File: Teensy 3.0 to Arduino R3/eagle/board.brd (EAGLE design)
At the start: 100 x 55.9 mm, 28 parts, among them IC1 7805TV

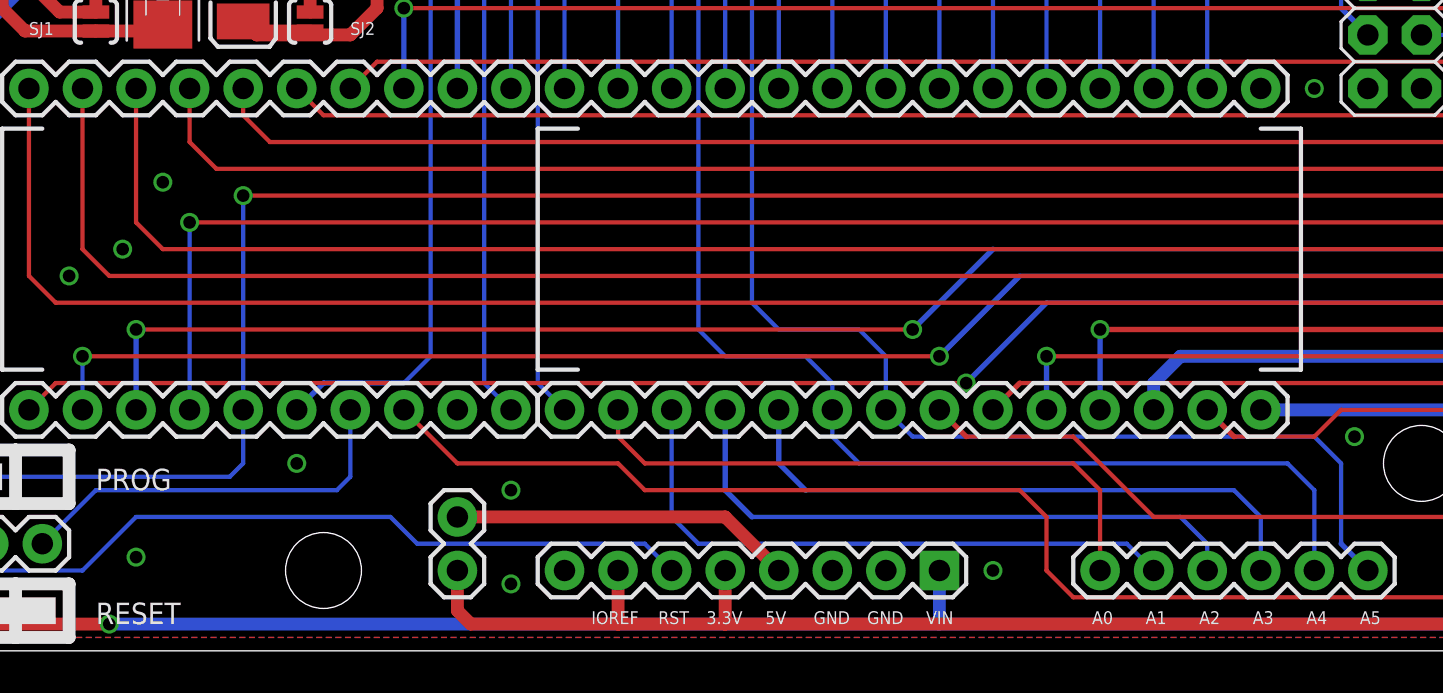
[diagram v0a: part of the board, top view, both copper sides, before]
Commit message: update Arduino R3 board
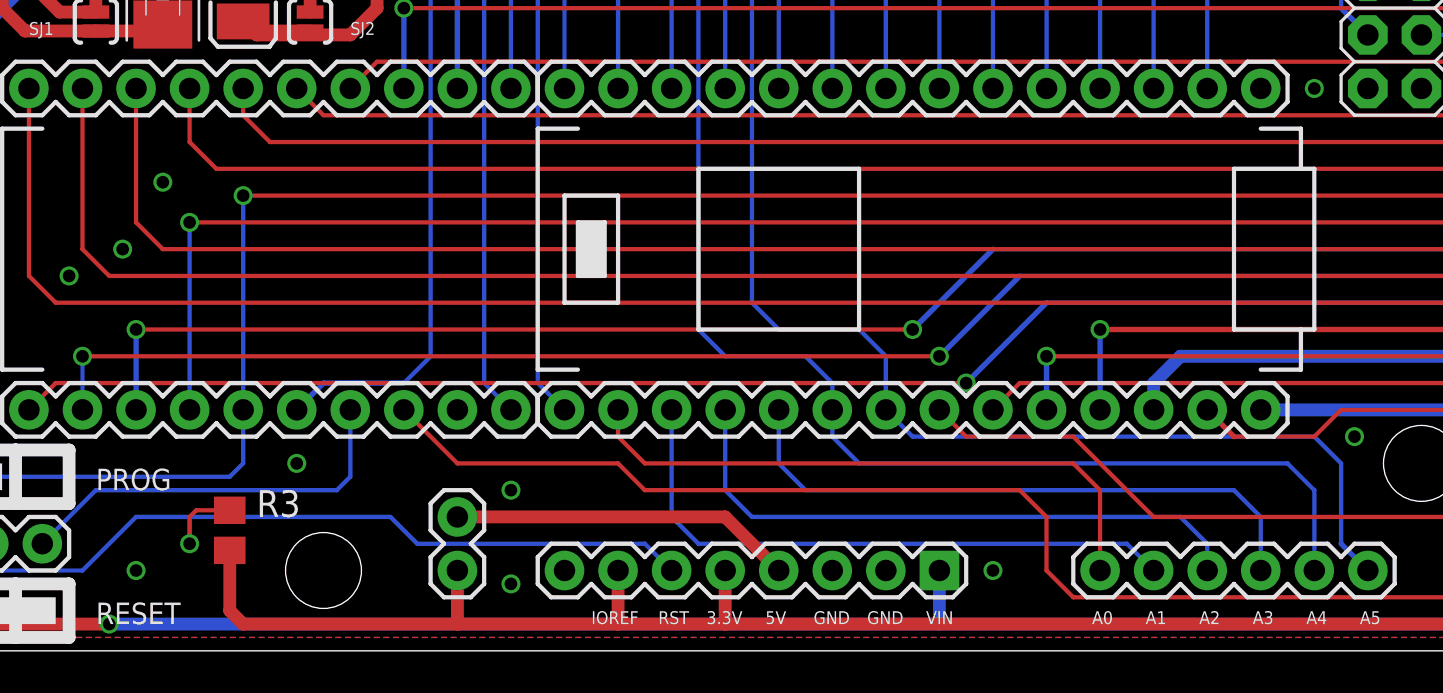
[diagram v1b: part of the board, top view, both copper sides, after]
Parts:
- added R3: (no value), rcl:R0805
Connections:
- net 3V3: now also R3.2
- net EXT_RESET: now also R3.1
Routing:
- net 3V3: track 275.3 -> 289.5 mm
- net EXT_RESET: track 49.5 -> 54.1 mm, vias 0 -> 1
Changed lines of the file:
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@@
 <wire x1="29.21" y1="50.165" x2="35.56" y2="50.165" width="0.2032" layer="21"/>
 <wire x1="35.56" y1="50.165" x2="35.56" y2="43.815" width="0.2032" layer="21"/>
-<wire x1="75.565" y1="24.765" x2="75.565" y2="13.335" width="0.2032" layer="21"/>
 <wire x1="75.565" y1="13.335" x2="73.66" y2="13.335" width="0.2032" layer="21"/>
 <wire x1="75.565" y1="24.765" x2="73.66" y2="24.765" width="0.2032" layer="21"/>
@@
 <text x="34.925" y="36.195" size="0.6096" layer="21">GND</text>
 <text x="34.925" y="33.655" size="0.6096" layer="21">VOUT</text>
+<wire x1="76.2" y1="22.86" x2="75.565" y2="22.86" width="0.2032" layer="21"/>
+<wire x1="75.565" y1="22.86" x2="72.39" y2="22.86" width="0.2032" layer="21"/>
+<wire x1="72.39" y1="22.86" x2="72.39" y2="15.24" width="0.2032" layer="21"/>
+<wire x1="76.2" y1="22.86" x2="76.2" y2="15.24" width="0.2032" layer="21"/>
+<wire x1="75.565" y1="24.765" x2="75.565" y2="22.86" width="0.2032" layer="21"/>
+<wire x1="40.64" y1="21.59" x2="40.64" y2="16.51" width="0.2032" layer="21"/>
+<wire x1="40.64" y1="16.51" x2="43.18" y2="16.51" width="0.2032" layer="21"/>
+<wire x1="43.18" y1="16.51" x2="43.18" y2="21.59" width="0.2032" layer="21"/>
+<wire x1="43.18" y1="21.59" x2="40.64" y2="21.59" width="0.2032" layer="21"/>
+<wire x1="41.275" y1="17.78" x2="42.545" y2="17.78" width="0.2032" layer="21"/>
+<wire x1="42.545" y1="17.78" x2="42.545" y2="20.32" width="0.2032" layer="21"/>
+<wire x1="42.545" y1="20.32" x2="41.275" y2="20.32" width="0.2032" layer="21"/>
+<wire x1="41.275" y1="20.32" x2="41.275" y2="17.78" width="0.2032" layer="21"/>
+<rectangle x1="41.275" y1="17.78" x2="42.545" y2="20.32" layer="21"/>
+<wire x1="46.99" y1="15.24" x2="54.61" y2="15.24" width="0.2032" layer="21"/>
+<wire x1="54.61" y1="15.24" x2="54.61" y2="22.86" width="0.2032" layer="21"/>
+<wire x1="54.61" y1="22.86" x2="46.99" y2="22.86" width="0.2032" layer="21"/>
+<wire x1="46.99" y1="22.86" x2="46.99" y2="15.24" width="0.2032" layer="21"/>
+<wire x1="72.39" y1="15.24" x2="75.565" y2="15.24" width="0.2032" layer="21"/>
+<wire x1="75.565" y1="15.24" x2="76.2" y2="15.24" width="0.2032" layer="21"/>
+<wire x1="75.565" y1="15.24" x2="75.565" y2="13.335" width="0.2032" layer="21"/>
 </plain>
 <attributes>
@@
 <attribute name="VALUE" x="38.735" y="2.54" size="1.27" layer="27" rot="R90"/>
 </element>
+<element name="R3" library="rcl" package="R0805" value="" x="24.765" y="5.715" smashed="yes" rot="R270">
+<attribute name="NAME" x="26.035" y="6.35" size="1.27" layer="25"/>
+<attribute name="VALUE" x="22.225" y="6.35" size="1.27" layer="27" rot="R270"/>
+</element>
 </elements>
 <signals>
@@
 <via x="60.96" y="3.81" extent="1-16" drill="0.6" shape="octagon"/>
 <via x="38.1" y="7.62" extent="1-16" drill="0.6" shape="octagon"/>
-<via x="20.32" y="4.445" extent="1-16" drill="0.6" shape="octagon"/>
 <via x="27.94" y="8.89" extent="1-16" drill="0.6" shape="octagon"/>
 <via x="17.145" y="17.78" extent="1-16" drill="0.6" shape="octagon"/>
@@
 <via x="75.565" y="35.56" extent="1-16" drill="0.6" shape="octagon"/>
 <via x="21.59" y="22.225" extent="1-16" drill="0.6" shape="octagon"/>
+<via x="20.32" y="3.81" extent="1-16" drill="0.6" shape="octagon"/>
 </signal>
 <signal name="D0">
@@
 <wire x1="43.18" y1="1.27" x2="43.18" y2="3.81" width="0.6096" layer="1"/>
 <wire x1="48.26" y1="3.81" x2="48.26" y2="1.27" width="0.6096" layer="1"/>
-<wire x1="35.56" y1="3.81" x2="35.56" y2="1.905" width="0.6096" layer="1"/>
-<wire x1="35.56" y1="1.905" x2="36.195" y2="1.27" width="0.6096" layer="1"/>
-<wire x1="36.195" y1="1.27" x2="43.18" y2="1.27" width="0.6096" layer="1"/>
+<contactref element="R3" pad="2"/>
+<wire x1="43.18" y1="1.27" x2="35.56" y2="1.27" width="0.6096" layer="1"/>
+<wire x1="35.56" y1="1.27" x2="25.4" y2="1.27" width="0.6096" layer="1"/>
+<wire x1="25.4" y1="1.27" x2="24.765" y2="1.905" width="0.6096" layer="1"/>
+<wire x1="24.765" y1="1.905" x2="24.765" y2="4.765" width="0.6096" layer="1"/>
+<wire x1="35.56" y1="3.81" x2="35.56" y2="1.27" width="0.6096" layer="1"/>
 </signal>
 <signal name="A9">
@@
 <wire x1="92.71" y1="10.16" x2="90.17" y2="12.7" width="0.2032" layer="1"/>
 <wire x1="90.17" y1="12.7" x2="62.23" y2="12.7" width="0.2032" layer="1"/>
-<wire x1="62.23" y1="12.7" x2="60.96" y2="11.43" width="0.254" layer="1"/>
+<wire x1="62.23" y1="12.7" x2="60.96" y2="11.43" width="0.2032" layer="1"/>
 <contactref element="JP13" pad="3"/>
 <wire x1="96.52" y1="11.43" x2="95.25" y2="10.16" width="0.2032" layer="1"/>
@@
 <wire x1="68.58" y1="6.35" x2="64.77" y2="10.16" width="0.2032" layer="1"/>
 <wire x1="64.77" y1="10.16" x2="59.69" y2="10.16" width="0.2032" layer="1"/>
-<wire x1="59.69" y1="10.16" x2="58.42" y2="11.43" width="0.254" layer="1"/>
+<wire x1="59.69" y1="10.16" x2="58.42" y2="11.43" width="0.2032" layer="1"/>
 <wire x1="68.58" y1="6.35" x2="88.9" y2="6.35" width="0.2032" layer="1"/>
 <wire x1="88.9" y1="6.35" x2="90.17" y2="7.62" width="0.2032" layer="1"/>
@@
 <wire x1="73.66" y1="6.35" x2="72.39" y2="7.62" width="0.2032" layer="16"/>
 <wire x1="72.39" y1="7.62" x2="52.07" y2="7.62" width="0.2032" layer="16"/>
-<wire x1="52.07" y1="7.62" x2="50.8" y2="8.89" width="0.254" layer="16"/>
-<wire x1="50.8" y1="8.89" x2="50.8" y2="11.43" width="0.254" layer="16"/>
+<wire x1="52.07" y1="7.62" x2="50.8" y2="8.89" width="0.2032" layer="16"/>
+<wire x1="50.8" y1="8.89" x2="50.8" y2="11.43" width="0.2032" layer="16"/>
 </signal>
 <signal name="A2">
@@
 <wire x1="71.12" y1="5.08" x2="69.85" y2="6.35" width="0.2032" layer="16"/>
 <wire x1="69.85" y1="6.35" x2="49.53" y2="6.35" width="0.2032" layer="16"/>
-<wire x1="49.53" y1="6.35" x2="48.26" y2="7.62" width="0.254" layer="16"/>
-<wire x1="48.26" y1="7.62" x2="48.26" y2="11.43" width="0.254" layer="16"/>
+<wire x1="49.53" y1="6.35" x2="48.26" y2="7.62" width="0.2032" layer="16"/>
+<wire x1="48.26" y1="7.62" x2="48.26" y2="11.43" width="0.2032" layer="16"/>
 </signal>
 <signal name="A1">
@@
 <wire x1="44.45" y1="5.08" x2="33.655" y2="5.08" width="0.2032" layer="16"/>
 <wire x1="33.655" y1="5.08" x2="32.385" y2="6.35" width="0.2032" layer="16"/>
-<wire x1="32.385" y1="6.35" x2="20.32" y2="6.35" width="0.2032" layer="16"/>
+<wire x1="32.385" y1="6.35" x2="22.86" y2="6.35" width="0.2032" layer="16"/>
+<contactref element="R3" pad="1"/>
+<wire x1="22.86" y1="6.35" x2="20.32" y2="6.35" width="0.2032" layer="16"/>
+<wire x1="24.765" y1="6.665" x2="23.175" y2="6.665" width="0.2032" layer="1"/>
+<wire x1="23.175" y1="6.665" x2="22.86" y2="6.35" width="0.2032" layer="1"/>
+<wire x1="22.86" y1="6.35" x2="22.86" y2="5.08" width="0.2032" layer="1"/>
+<via x="22.86" y="5.08" extent="1-16" drill="0.6" shape="octagon"/>
+<wire x1="22.86" y1="5.08" x2="22.86" y2="6.35" width="0.2032" layer="16"/>
 </signal>
 </signals>

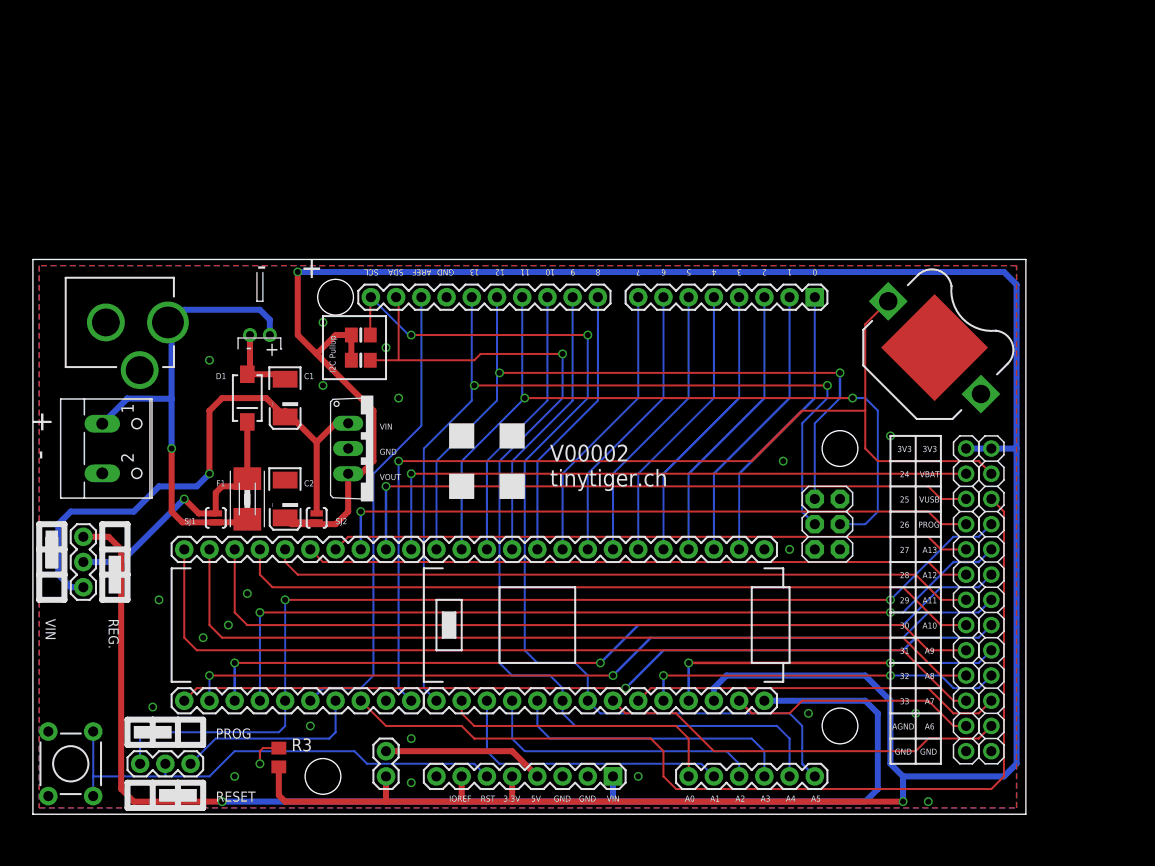
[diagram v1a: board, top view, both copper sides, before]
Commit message: update: -Arduino R3 pcb - breadboard pcb
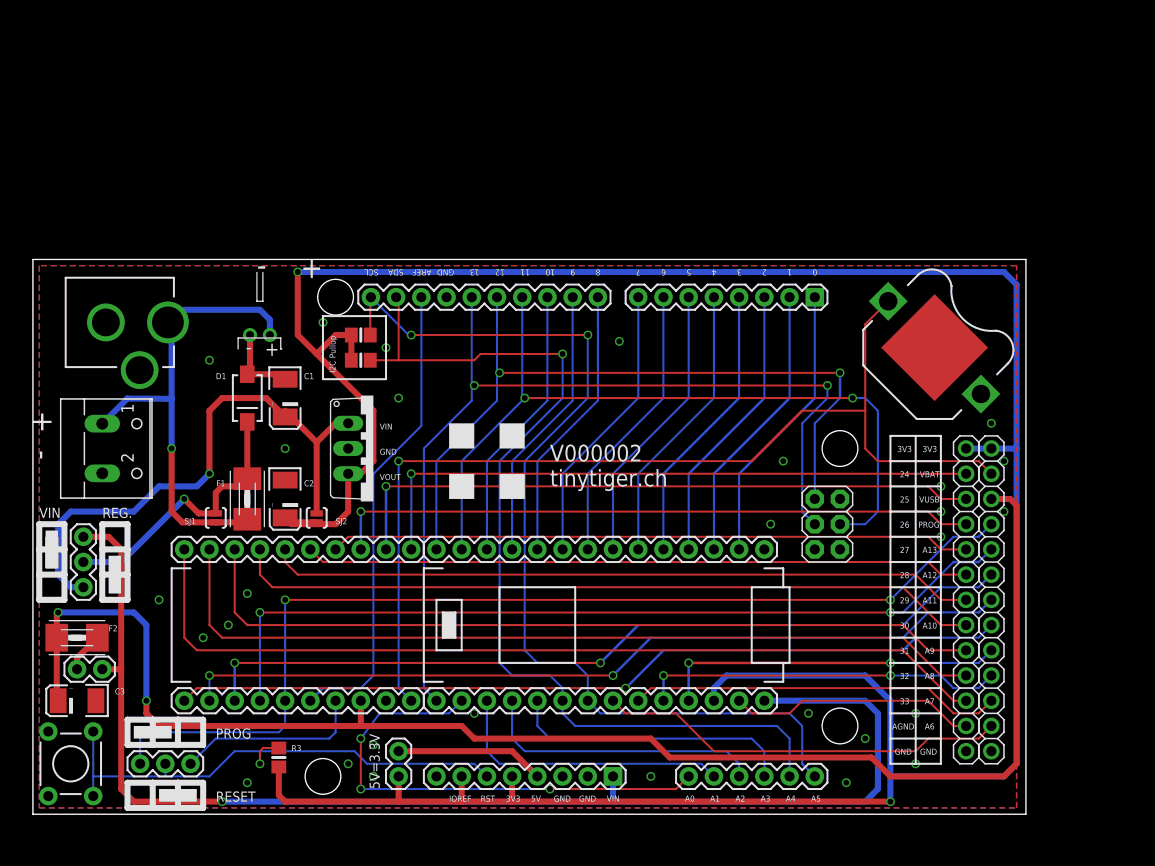
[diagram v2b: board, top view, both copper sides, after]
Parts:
- added C3: (no value), SparkFun-Capacitors:EIA3528-KIT
- added F2: (no value), adafruit:1812
- added JP15: (no value), SparkFun-Connectors:1X02
- moved JP14 1.27 mm to (36.8, 3.81)
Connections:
- new net N$2: F2.2, JP15.2
- net GND: now also C3.C
- net VIN: now also JP15.1
- net VUSB: now also C3.A, F2.1
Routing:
- net VUSB: track 98.9 -> 149.5 mm, vias 0 -> 2
- net A0: track 29.0 -> 50.6 mm, vias 0 -> 3
- net N$2: track 0.00 -> 4.02 mm
- net VIN: track 127.8 -> 129.7 mm
- net 5V: track 16.3 -> 15.0 mm
- net 3V3: track 289.5 -> 289.0 mm
- net GND: vias 21 -> 29
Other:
- board text added: "5V=3.3V"
- board text added: "C3"
- board text added: "F2"
- board text added: "V000002 tinytiger.ch"
- board text removed: "3.3V"
- board text removed: "V00002 tinytiger.ch"

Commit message: added i2c eeprom, sdcard
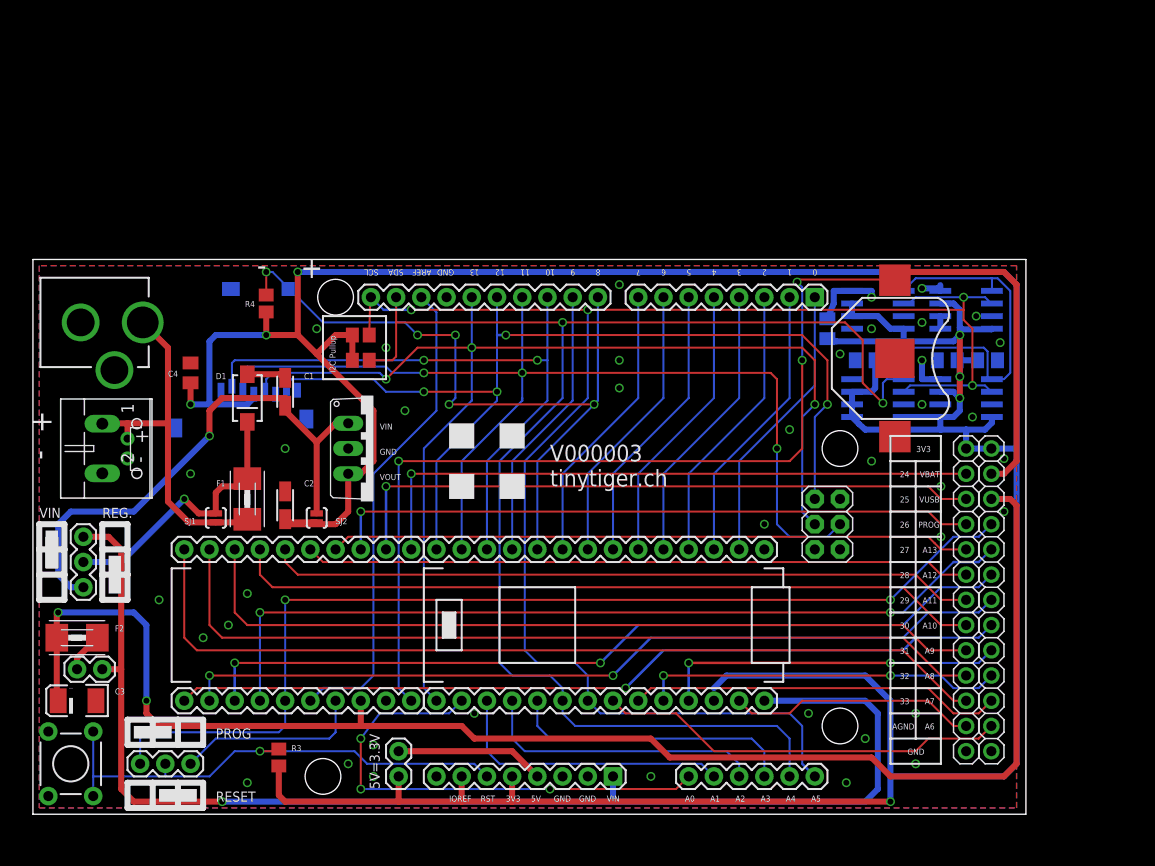
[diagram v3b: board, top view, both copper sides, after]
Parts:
- added C4, C5, C6, C7, C8: (no value), rcl:C0805K
- added IC2, IC3, IC4, IC5: 24AA256SN, microchip:SO-08
- added R4: (no value), resistor:R0805
- added U1: MICROSD, adafruit:MICROSD
- BAT1: device SparkFun-Electromechanical:BATTCON_12MM_PTH -> SparkFun-Electromechanical:BATTCON_12MM
- C1, C2: device SparkFun-Capacitors:EIA3528-KIT -> resistor:CT3216
- R1, R2, R3: device rcl:R0805 -> resistor:R0805
- moved CN1 17.6 mm to (9.53, 36.8), turned to 90 degrees
- moved BAT1 4.14 mm to (86.8, 45.9), turned to 270 degrees
- moved CN2 2.54 mm to (-2.54, 49.5)
- moved C1 0.64 mm to (25.4, 42.5)
- moved C2 0.64 mm to (25.4, 31.1)
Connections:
- new net 3.3V: JP2.12
- net 3V3: now also C2.+, C4.1, C5.1, C6.1, C7.1, C8.1, IC2.3, IC2.8, IC3.2, IC3.3, IC3.8, IC4.1, IC4.3, IC4.8, IC5.1, IC5.2, IC5.3, IC5.8, R4.2, U1.4; no longer C2.A, JP2.12
- net A4: now also IC2.5, IC3.5, IC4.5, IC5.5
- net A5: now also IC2.6, IC3.6, IC4.6, IC5.6
- net D10: now also U1.2
- net D11: now also U1.3
- net D12: now also U1.7
- net D13: now also U1.5
- net D8: now also R4.1, U1.CD1
- net GND: now also C1.-, C2.-, C4.2, C5.2, C6.2, C7.2, C8.2, IC2.1, IC2.2, IC2.4, IC2.7, IC3.1, IC3.4, IC3.7, IC4.2, IC4.4, IC4.7, IC5.4, IC5.7, U1.6, U1.MT1, U1.MT2; no longer C1.C, C2.C
- net N$3: now also C1.+; no longer C1.A
- net VBAT: now also BAT1.PWR@1; no longer BAT1.VCC@1
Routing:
- net 3V3: track 289.0 -> 390.8 mm, vias 2 -> 7
- net A4: track 97.5 -> 182.5 mm, vias 1 -> 2
- net A5: track 99.8 -> 166.6 mm, vias 2 -> 4
- net D8: track 27.9 -> 73.9 mm, vias 0 -> 5
- net D10: track 27.9 -> 62.2 mm, vias 0 -> 2
- net D11: track 78.8 -> 106.4 mm, vias 2 -> 3
- net D13: track 94.5 -> 119.5 mm, vias 2 -> 3
- net VBAT: track 103.3 -> 126.6 mm, vias 1 -> 3
- net D12: track 76.2 -> 99.3 mm, vias 2 -> 4
- net EXT_POWER: track 48.2 -> 36.3 mm, vias 1 -> 0
- net GND: track 8.08 -> 19.2 mm, vias 29 -> 40
- net EXT_RESET: track 54.1 -> 51.5 mm
- net N$3: track 56.4 -> 54.1 mm
- net AREF: track 47.5 -> 48.8 mm
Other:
- board text added: "Teensy 3.0 to Arduino R3 adapter This work is licensed under a Creative Commons Attribution-ShareAlike 3.0 Unported License. http://creativecommons.org/licenses/by-sa/3.0/ (c) 2012 Jonas Niggli (thewknd)"
- board text added: "V000003 tinytiger.ch"
- board text removed: "V000002 tinytiger.ch"
